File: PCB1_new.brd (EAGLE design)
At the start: 101.4 x 47.5 mm, 73 parts

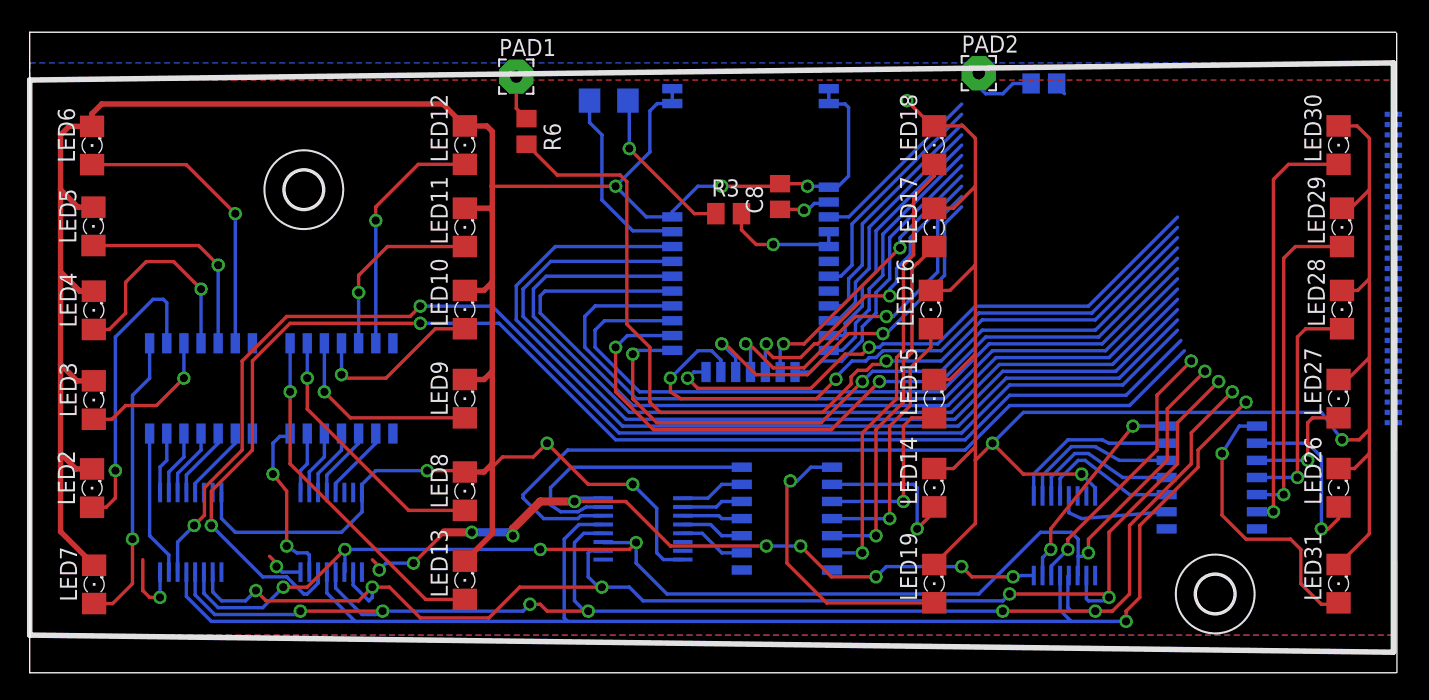
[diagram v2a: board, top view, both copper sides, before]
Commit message: Finished changes to PCB1 by switching out resistor packages and reordering the pin connections for PCB2
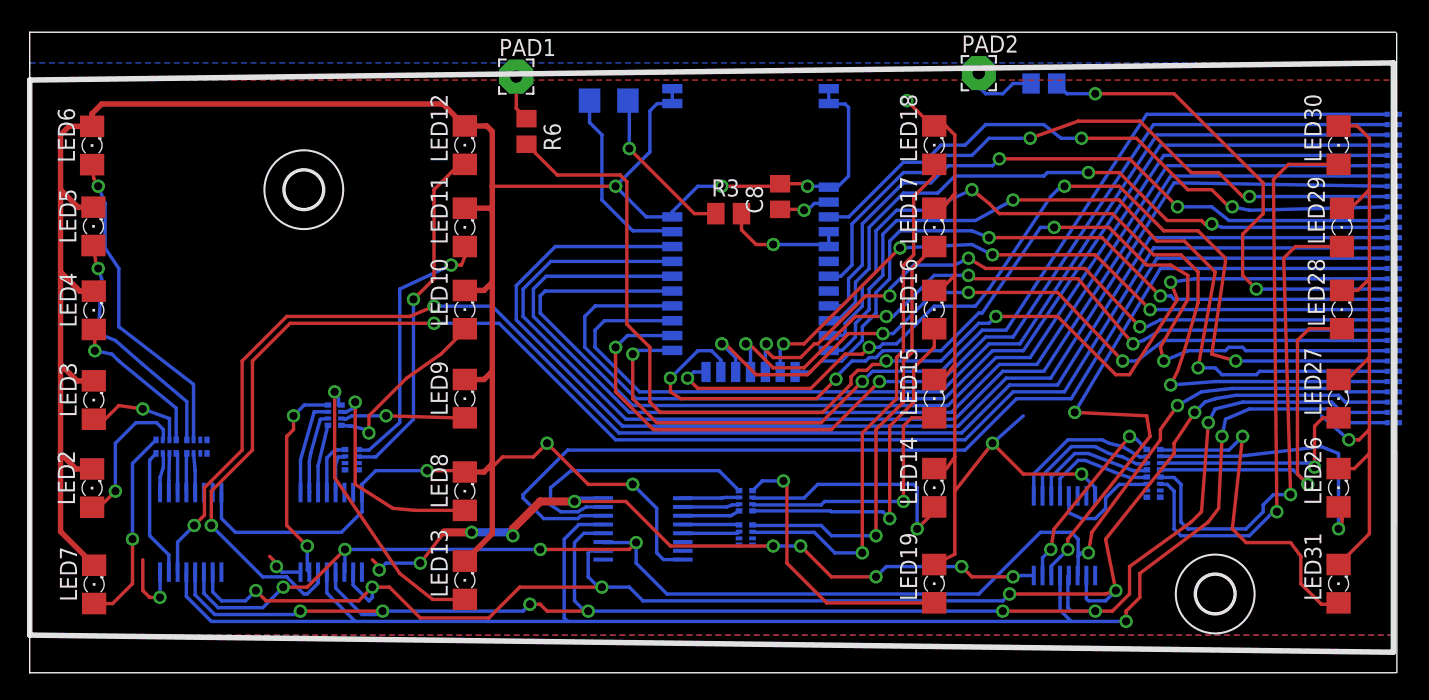
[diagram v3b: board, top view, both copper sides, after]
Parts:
- removed R1, R2, R4, R5: (no value), resistor-bourns:4814P
- added U$37, U$38, U$39, U$40, U$41, U$42, U$43, U$44: MNR04MRAPJ680, ECE477_Guitutar:MNR04
- moved LED16 0.25 mm to (67.1, 26.9)
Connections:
- removed net N$20: R2.12, U$1.2
- removed net N$28: LED10.A, R2.4
- removed net N$46: LED16.A, R4.4
- removed net N$70: LED28.A, R5.4
- new net N$13: U$1.1, U$39.P$6
- new net N$14: U$1.2, U$39.P$7
- new net N$17: LED10.A, U$39.P$4
- new net N$18: LED16.A, U$41.P$4
- net N$1: now also U$37.P$6; no longer R1.13
- net N$10: now also U$37.P$4; no longer R1.4
- net N$11: now also U$38.P$1; no longer R1.5
- net N$12: now also U$38.P$2; no longer R1.6
- net N$19: now also LED28.A, U$43.P$4; no longer R2.13, U$1.1
- net N$2: now also U$37.P$7; no longer R1.12
- net N$21: now also U$39.P$8; no longer R2.11
- net N$22: now also U$40.P$5; no longer R2.10
- net N$23: now also U$40.P$6; no longer R2.9
- net N$24: now also U$39.P$5; no longer R2.14
- net N$25: now also U$39.P$1; no longer R2.1
- net N$26: now also U$39.P$2; no longer R2.2
- net N$27: now also U$39.P$3; no longer R2.3
- net N$29: now also U$40.P$1; no longer R2.5
- net N$3: now also U$37.P$8; no longer R1.11
- net N$30: now also U$40.P$2; no longer R2.6
- net N$35: now also U$41.P$6; no longer R4.13
- net N$36: now also U$41.P$7; no longer R4.12
- net N$37: now also U$41.P$8; no longer R4.11
- net N$38: now also U$42.P$5; no longer R4.10
- net N$39: now also U$42.P$6; no longer R4.9
- net N$4: now also U$38.P$5; no longer R1.10
- net N$40: now also U$41.P$5; no longer R4.14
- net N$41: now also U$41.P$1; no longer R4.1
- net N$43: now also U$41.P$2; no longer R4.2
- net N$44: now also U$41.P$3; no longer R4.3
- net N$47: now also U$42.P$1; no longer R4.5
- net N$49: now also U$42.P$2; no longer R4.6
- net N$5: now also U$38.P$6; no longer R1.9
- net N$6: now also U$37.P$1; no longer R1.1
- net N$60: now also U$43.P$6; no longer R5.13
- net N$61: now also U$43.P$7; no longer R5.12
- net N$62: now also U$43.P$8; no longer R5.11
- net N$63: now also U$44.P$5; no longer R5.10
- net N$64: now also U$44.P$6; no longer R5.9
- net N$66: now also U$43.P$5; no longer R5.14
- net N$67: now also U$43.P$1; no longer R5.1
- net N$68: now also U$43.P$2; no longer R5.2
- net N$69: now also U$43.P$3; no longer R5.3
- net N$7: now also U$37.P$5; no longer R1.14
- net N$71: now also U$44.P$1; no longer R5.5
- net N$72: now also U$44.P$2; no longer R5.6
- net N$8: now also U$37.P$2; no longer R1.2
- net N$9: now also U$37.P$3; no longer R1.3
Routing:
- net FRET1: track 45.4 -> 90.6 mm, vias 1 -> 3
- net P1_2: track 18.8 -> 61.9 mm, vias 0 -> 2
- net P1_3: track 19.1 -> 60.2 mm, vias 0 -> 2
- net SW_BTN: track 13.3 -> 46.7 mm, vias 0 -> 2
- net WAKEUP: track 16.6 -> 50.0 mm, vias 0 -> 2
- net P0_4: track 18.1 -> 50.5 mm, vias 0 -> 2
- net P1_5: track 18.2 -> 50.3 mm, vias 0 -> 2
- net P1_7: track 22.0 -> 53.4 mm, vias 0 -> 2
- net P0_5: track 21.0 -> 51.8 mm, vias 2 -> 4
- net P0_0: track 24.2 -> 54.3 mm, vias 2 -> 4
- net P2_4: track 28.6 -> 58.3 mm, vias 2 -> 4
- net P2_0: track 26.5 -> 56.0 mm, vias 2 -> 4
- net LED_SER4: track 20.2 -> 49.1 mm
- net GND: track 353.0 -> 324.2 mm
- net RST_N: track 43.5 -> 71.3 mm, vias 2 -> 4
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
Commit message: Moved resistor and fret pad on PCB1_new
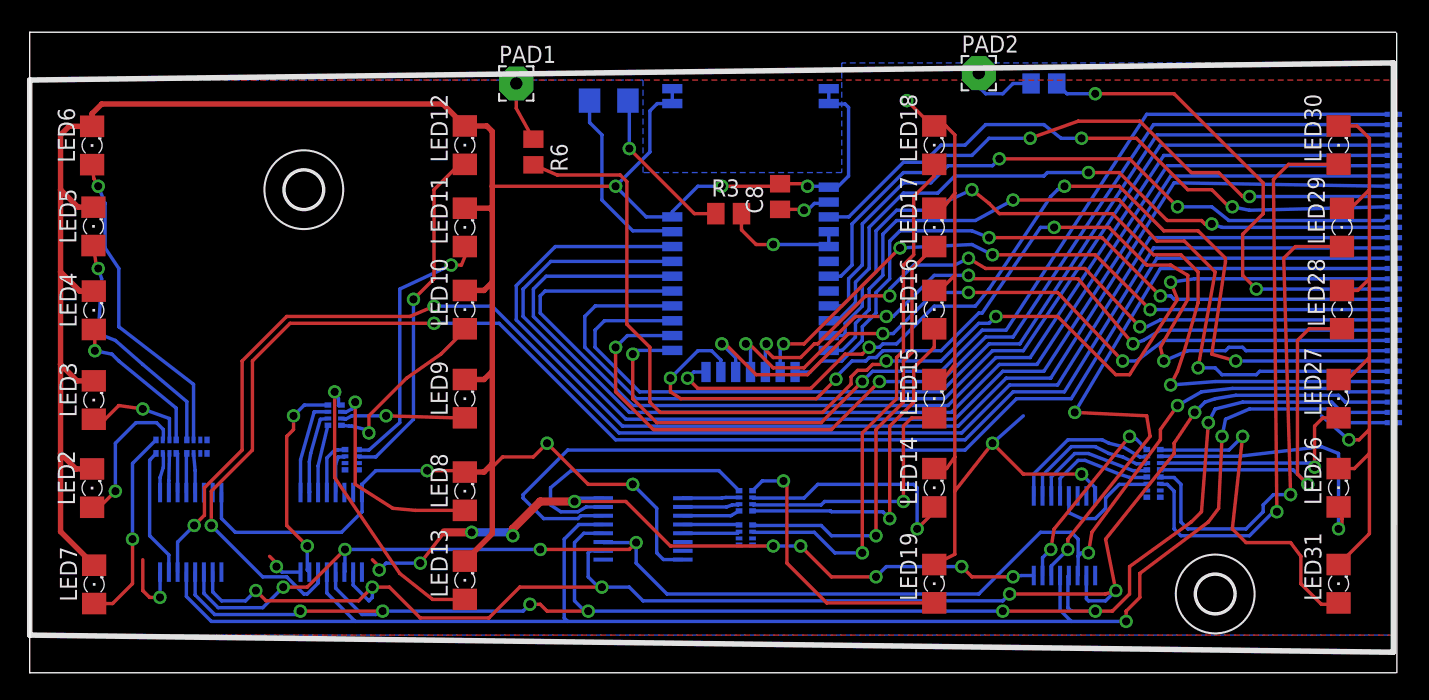
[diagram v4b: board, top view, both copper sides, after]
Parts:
- moved R6 1.61 mm to (37.3, 38.6)
- moved PAD1 0.51 mm to (36.1, 43.7)
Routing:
- net FRET1: track 90.6 -> 89.3 mm
- net N$116: track 3.43 -> 4.46 mm
- added copper zone on layer 16, net N$20
- removed copper zone on layer 16, net GND
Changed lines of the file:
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@@
 <?xml version="1.0" encoding="utf-8"?>
 <!DOCTYPE eagle SYSTEM "eagle.dtd">
-<eagle version="8.0.1">
+<eagle version="8.1.0">
 <drawing>
 <settings>
@@
 <element name="U$4" library="ECE477_Guitutar" package="MM74HC595MTCXCT-ND" value="MM74HC595TSSOP-LD16" x="11.938" y="10.414" rot="MR180"/>
 <element name="U$5" library="ECE477_Guitutar" package="MM74HC595MTCXCT-ND" value="MM74HC595TSSOP-LD16" x="76.708" y="10.16" rot="MR180"/>
-<element name="PAD1" library="wirepad" package="2,54/0,9" value="WIREPAD2,54/0,9" x="36.068" y="44.196"/>
+<element name="PAD1" library="wirepad" package="2,54/0,9" value="WIREPAD2,54/0,9" x="36.068" y="43.688"/>
 <element name="PAD2" library="wirepad" package="2,54/0,9" value="WIREPAD2,54/0,9" x="70.358" y="44.45"/>
 <element name="U$2" library="ECE477_Guitutar" package="BM78SPP05MC2/NC2" value="BM78SPP05MC2/NC2" x="59.436" y="22.098" rot="MR0"/>
@@
 <element name="H1" library="holes" package="2,8" value="MOUNT-HOLE2.8" x="20.32" y="35.814"/>
 <element name="H2" library="holes" package="2,8" value="MOUNT-HOLE2.8" x="87.884" y="5.842"/>
-<element name="R6" library="rcl" package="R0805" value="330k" x="36.83" y="40.132" rot="R270"/>
+<element name="R6" library="rcl" package="R0805" value="330k" x="37.338" y="38.608" rot="R270"/>
 <element name="R7" library="rcl" package="R0805" value="330k" x="75.184" y="43.688" rot="MR180"/>
 <element name="U$37" library="ECE477_Guitutar" package="MNR04" value="MNR04MRAPJ680" x="10.16" y="16.764" rot="MR180"/>
@@
 <wire x1="38.354" y1="17.018" x2="37.338" y2="16.002" width="0.254" layer="1"/>
 <via x="38.354" y="17.018" extent="1-16" drill="0.6"/>
-<polygon width="0.254" layer="16">
-<vertex x="0" y="45.212"/>
-<vertex x="101.092" y="45.212"/>
-<vertex x="101.092" y="2.794"/>
-<vertex x="0" y="2.794"/>
-</polygon>
 <wire x1="24.627" y1="13.364" x2="24.627" y2="13.959" width="0.254" layer="16"/>
 <wire x1="24.627" y1="13.959" x2="25.654" y2="14.986" width="0.254" layer="16"/>
@@
 <wire x1="73.66" y1="14.732" x2="71.374" y2="17.018" width="0.254" layer="1"/>
 <wire x1="77.978" y1="14.732" x2="73.66" y2="14.732" width="0.254" layer="1"/>
+<wire x1="78.983" y1="13.727" x2="95.758" y2="19.05" width="0" layer="19" extent="16-16"/>
+<wire x1="60.706" y1="41.91" x2="65.024" y2="42.418" width="0" layer="19" extent="16-16"/>
 </signal>
 <signal name="G">
@@
 <contactref element="U$1" pad="3"/>
 <contactref element="U$39" pad="P$8"/>
-<wire x1="21.377" y1="13.364" x2="21.274" y2="13.467" width="0" layer="19" extent="1-16"/>
 <wire x1="22.106" y1="18.35" x2="21.377" y2="15.335" width="0.254" layer="16"/>
 <wire x1="21.377" y1="15.335" x2="21.377" y2="13.364" width="0.254" layer="16"/>
@@
 <wire x1="56.134" y1="13.97" x2="55.88" y2="14.224" width="0.254" layer="1"/>
 <via x="55.88" y="14.224" extent="1-16" drill="0.6"/>
-<wire x1="55.88" y1="14.224" x2="56.896" y2="14.224" width="0" layer="19" extent="1-16"/>
-<wire x1="56.896" y1="14.224" x2="57.912" y2="15.24" width="0" layer="19" extent="1-16"/>
 <contactref element="U$41" pad="P$1"/>
 <wire x1="53.586" y1="13.5" x2="54.31" y2="14.224" width="0.254" layer="16"/>
@@
 <wire x1="83.812" y1="16.548" x2="83.85" y2="16.51" width="0.254" layer="16"/>
 <wire x1="83.85" y1="16.51" x2="88.9" y2="16.51" width="0.254" layer="16"/>
-<wire x1="89.154" y1="14.224" x2="89.154" y2="14.224" width="0" layer="19" extent="1-16"/>
 </signal>
 <signal name="N$68">
@@
 <contactref element="PAD1" pad="1"/>
 <contactref element="R6" pad="1"/>
-<wire x1="36.068" y1="44.196" x2="36.068" y2="41.844" width="0.254" layer="1"/>
-<wire x1="36.068" y1="41.844" x2="36.83" y2="41.082" width="0.254" layer="1"/>
+<wire x1="36.068" y1="43.688" x2="36.068" y2="41.844" width="0.254" layer="1"/>
+<wire x1="36.068" y1="41.844" x2="37.338" y2="39.558" width="0.254" layer="1"/>
 </signal>
 <signal name="N$117">
@@
 <contactref element="R6" pad="2"/>
 <wire x1="43.77920625" y1="36.9014" x2="44.2674" y2="36.41320625" width="0.254" layer="1"/>
-<wire x1="36.83" y1="39.182" x2="39.1106" y2="36.9014" width="0.254" layer="1"/>
+<wire x1="37.338" y1="37.658" x2="39.1106" y2="36.9014" width="0.254" layer="1"/>
 <wire x1="39.1106" y1="36.9014" x2="43.77920625" y2="36.9014" width="0.254" layer="1"/>
 <wire x1="44.2674" y1="36.41320625" x2="44.2674" y2="25.8366" width="0.254" layer="1"/>
@@
 <wire x1="93.664" y1="15.048" x2="94.742" y2="13.97" width="0.254" layer="16"/>
 </signal>
+<signal name="N$20">
+<polygon width="0.4064" layer="16">
+<vertex x="0" y="2.794"/>
+<vertex x="101.092" y="2.794"/>
+<vertex x="101.092" y="45.212"/>
+<vertex x="60.198" y="45.212"/>
+<vertex x="60.198" y="37.084"/>
+<vertex x="45.466" y="37.084"/>
+<vertex x="45.466" y="43.942"/>
+<vertex x="0" y="43.942"/>
+</polygon>
+</signal>
 </signals>

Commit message: Modifying dimensions on PCB#_new boards
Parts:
- moved U$34 0.71 mm to (101.1, 41.4)
- moved U$35 0.58 mm to (101.1, 42.0)
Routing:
- net N$67: track 24.9 -> 23.9 mm
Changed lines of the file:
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@@
 <setting verticaltext="up"/>
 </settings>
-<grid distance="0.01" unitdist="inch" unit="inch" style="lines" multiple="1" display="no" altdistance="0.025" altunitdist="inch" altunit="inch"/>
+<grid distance="0.001" unitdist="inch" unit="inch" style="lines" multiple="1" display="yes" altdistance="0.025" altunitdist="inch" altunit="inch"/>
 <layers>
 <layer number="1" name="Top" color="4" fill="1" visible="yes" active="yes"/>
@@
 <wire x1="101.27" y1="47.488" x2="0" y2="47.488" width="0" layer="20"/>
 <wire x1="0" y1="47.488" x2="0" y2="0" width="0" layer="20"/>
-<wire x1="0" y1="2.794" x2="101.092" y2="1.524" width="0.4064" layer="21"/>
-<wire x1="101.092" y1="1.524" x2="101.092" y2="45.212" width="0.4064" layer="21"/>
-<wire x1="101.092" y1="45.212" x2="0" y2="43.942" width="0.4064" layer="21"/>
+<wire x1="0" y1="2.794" x2="101.092" y2="1.9812" width="0.4064" layer="21"/>
+<wire x1="101.092" y1="1.9812" x2="101.092" y2="44.7548" width="0.4064" layer="21"/>
+<wire x1="101.092" y1="44.7548" x2="0" y2="43.942" width="0.4064" layer="21"/>
 <wire x1="0" y1="43.942" x2="0" y2="2.794" width="0.4064" layer="21"/>
 <wire x1="101.336" y1="47.422" x2="101.356" y2="0" width="0" layer="20"/>
 <dimension x1="101.092" y1="45.212" x2="101.092" y2="42.926" x3="104.902" y3="44.069" textsize="1.778" layer="16" dtype="vertical"/>
+<dimension x1="0" y1="43.942" x2="0" y2="2.794" x3="-4.064" y3="23.368" textsize="1.778" layer="1"/>
+<dimension x1="101.092" y1="1.9812" x2="101.4222" y2="44.7548" x3="116.9416" y3="23.368" textsize="1.778" layer="16" dtype="vertical"/>
+<dimension x1="102.0318" y1="44.7548" x2="102.7684" y2="41.9862" x3="99.4918" y3="43.3705" textsize="1.778" layer="16" dtype="vertical"/>
+<dimension x1="102.4636" y1="41.9862" x2="102.6668" y2="41.3512" x3="102.616" y3="41.6687" textsize="1.778" layer="16" dtype="vertical"/>
+<dimension x1="101.546" y1="41.3512" x2="102.4636" y2="40.7162" x3="102.235" y3="41.0337" textsize="1.778" layer="16" dtype="vertical"/>
 </plain>
 <attributes>
@@
 <element name="U$32" library="ECE477_Guitutar" package="JUMPER" value="JUMPER" x="101.092" y="20.828" rot="MR0"/>
 <element name="U$33" library="ECE477_Guitutar" package="JUMPER" value="JUMPER" x="101.092" y="39.878" rot="MR0"/>
-<element name="U$34" library="ECE477_Guitutar" package="JUMPER" value="JUMPER" x="101.092" y="40.64" rot="MR0"/>
-<element name="U$35" library="ECE477_Guitutar" package="JUMPER" value="JUMPER" x="101.092" y="41.402" rot="MR0"/>
+<element name="U$34" library="ECE477_Guitutar" package="JUMPER" value="JUMPER" x="101.092" y="41.3512" rot="MR0"/>
+<element name="U$35" library="ECE477_Guitutar" package="JUMPER" value="JUMPER" x="101.092" y="41.9862" rot="MR0"/>
 <element name="U$36" library="ECE477_Guitutar" package="JUMPER" value="JUMPER" x="101.092" y="20.066" rot="MR0"/>
 <element name="H1" library="holes" package="2,8" value="MOUNT-HOLE2.8" x="20.32" y="35.814"/>
@@
 <wire x1="76.383" y1="4.643" x2="77.216" y2="3.81" width="0.254" layer="16"/>
 <via x="81.28" y="3.81" extent="1-16" drill="0.6"/>
-<via x="88.392" y="17.526" extent="1-16" drill="0.6"/>
+<via x="88.4936" y="18.034" extent="1-16" drill="0.6"/>
 <wire x1="77.216" y1="3.81" x2="81.28" y2="3.81" width="0.254" layer="16"/>
 <wire x1="81.28" y1="3.81" x2="81.28" y2="4.572" width="0.254" layer="1"/>
@@
 <wire x1="82.296" y1="7.366" x2="87.376" y2="11.176" width="0.254" layer="1"/>
 <wire x1="87.376" y1="11.176" x2="88.138" y2="12.192" width="0.254" layer="1"/>
-<wire x1="88.138" y1="12.192" x2="88.392" y2="17.526" width="0.254" layer="1"/>
+<wire x1="88.138" y1="12.192" x2="88.4936" y2="18.034" width="0.254" layer="1"/>
 <contactref element="U$30" pad="P$2"/>
 <contactref element="U$30" pad="P$1"/>
@@
 <wire x1="100.638" y1="18.542" x2="97.282" y2="18.542" width="0.254" layer="16"/>
 <wire x1="90.424" y1="19.558" x2="88.646" y2="18.796" width="0.254" layer="16"/>
-<wire x1="88.646" y1="18.796" x2="88.392" y2="17.526" width="0.254" layer="16"/>
+<wire x1="88.646" y1="18.796" x2="88.4936" y2="18.034" width="0.254" layer="16"/>
 <wire x1="100.638" y1="18.542" x2="101.546" y2="18.542" width="0" layer="19" extent="16-16"/>
 </signal>
@@
 <signal name="N$67">
 <contactref element="LED31" pad="A"/>
-<wire x1="88.9" y1="16.51" x2="89.916" y2="17.526" width="0.254" layer="16"/>
-<via x="89.916" y="17.526" extent="1-16" drill="0.6"/>
+<wire x1="88.9" y1="16.51" x2="89.8144" y2="16.891" width="0.254" layer="16"/>
+<via x="89.8144" y="16.891" extent="1-16" drill="0.6"/>
 <wire x1="97.028" y1="5.182" x2="96.926" y2="5.08" width="0.254" layer="1"/>
 <wire x1="96.926" y1="5.08" x2="95.758" y2="5.08" width="0.254" layer="1"/>
@@
 <wire x1="93.472" y1="9.652" x2="90.17" y2="9.652" width="0.254" layer="1"/>
 <wire x1="90.17" y1="9.652" x2="89.154" y2="10.668" width="0.254" layer="1"/>
-<wire x1="89.154" y1="10.668" x2="89.916" y2="17.526" width="0.254" layer="1"/>
+<wire x1="89.154" y1="10.668" x2="89.8144" y2="16.891" width="0.254" layer="1"/>
 <contactref element="U$43" pad="P$1"/>
 <wire x1="83.812" y1="16.548" x2="83.85" y2="16.51" width="0.254" layer="16"/>
@@
 <contactref element="U$35" pad="P$2"/>
 <contactref element="U$35" pad="P$1"/>
-<wire x1="82.804" y1="41.402" x2="100.638" y2="41.402" width="0.254" layer="16"/>
+<wire x1="82.804" y1="41.402" x2="100.638" y2="41.9862" width="0.254" layer="16"/>
 <wire x1="72.39" y1="25.4" x2="82.804" y2="41.402" width="0.254" layer="16"/>
-<wire x1="100.638" y1="41.402" x2="101.546" y2="41.402" width="0" layer="19" extent="16-16"/>
+<wire x1="100.638" y1="41.9862" x2="101.546" y2="41.9862" width="0" layer="19" extent="16-16"/>
 </signal>
 <signal name="TXD">
@@
 <contactref element="U$34" pad="P$2"/>
 <contactref element="U$34" pad="P$1"/>
-<wire x1="83.312" y1="40.64" x2="100.638" y2="40.64" width="0.254" layer="16"/>
+<wire x1="83.312" y1="40.64" x2="100.638" y2="41.3512" width="0.254" layer="16"/>
 <wire x1="72.898" y1="24.892" x2="83.312" y2="40.64" width="0.254" layer="16"/>
-<wire x1="100.638" y1="40.64" x2="101.546" y2="40.64" width="0" layer="19" extent="16-16"/>
+<wire x1="100.638" y1="41.3512" x2="101.546" y2="41.3512" width="0" layer="19" extent="16-16"/>
 </signal>
 <signal name="P3_1">
